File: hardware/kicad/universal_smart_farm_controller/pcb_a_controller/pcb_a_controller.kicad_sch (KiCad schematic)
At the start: 55 parts, among them J1 Conn_01x12, J19 Conn_01x03, J2 Conn_01x03, J3 Conn_01x04, J4 Conn_01x04, J5 Conn_01x03, J6 Conn_01x03, J7 Conn_01x03, J8 Conn_01x03, J9 Conn_01x04, SW1 RESET, SW2 BOOT, U1 ESP32-WROOM-32E, U2 ADS1115IDGS, U3 MAX3485ESA+, U4 TPS5430DDA, U5 AP2112K-3.3

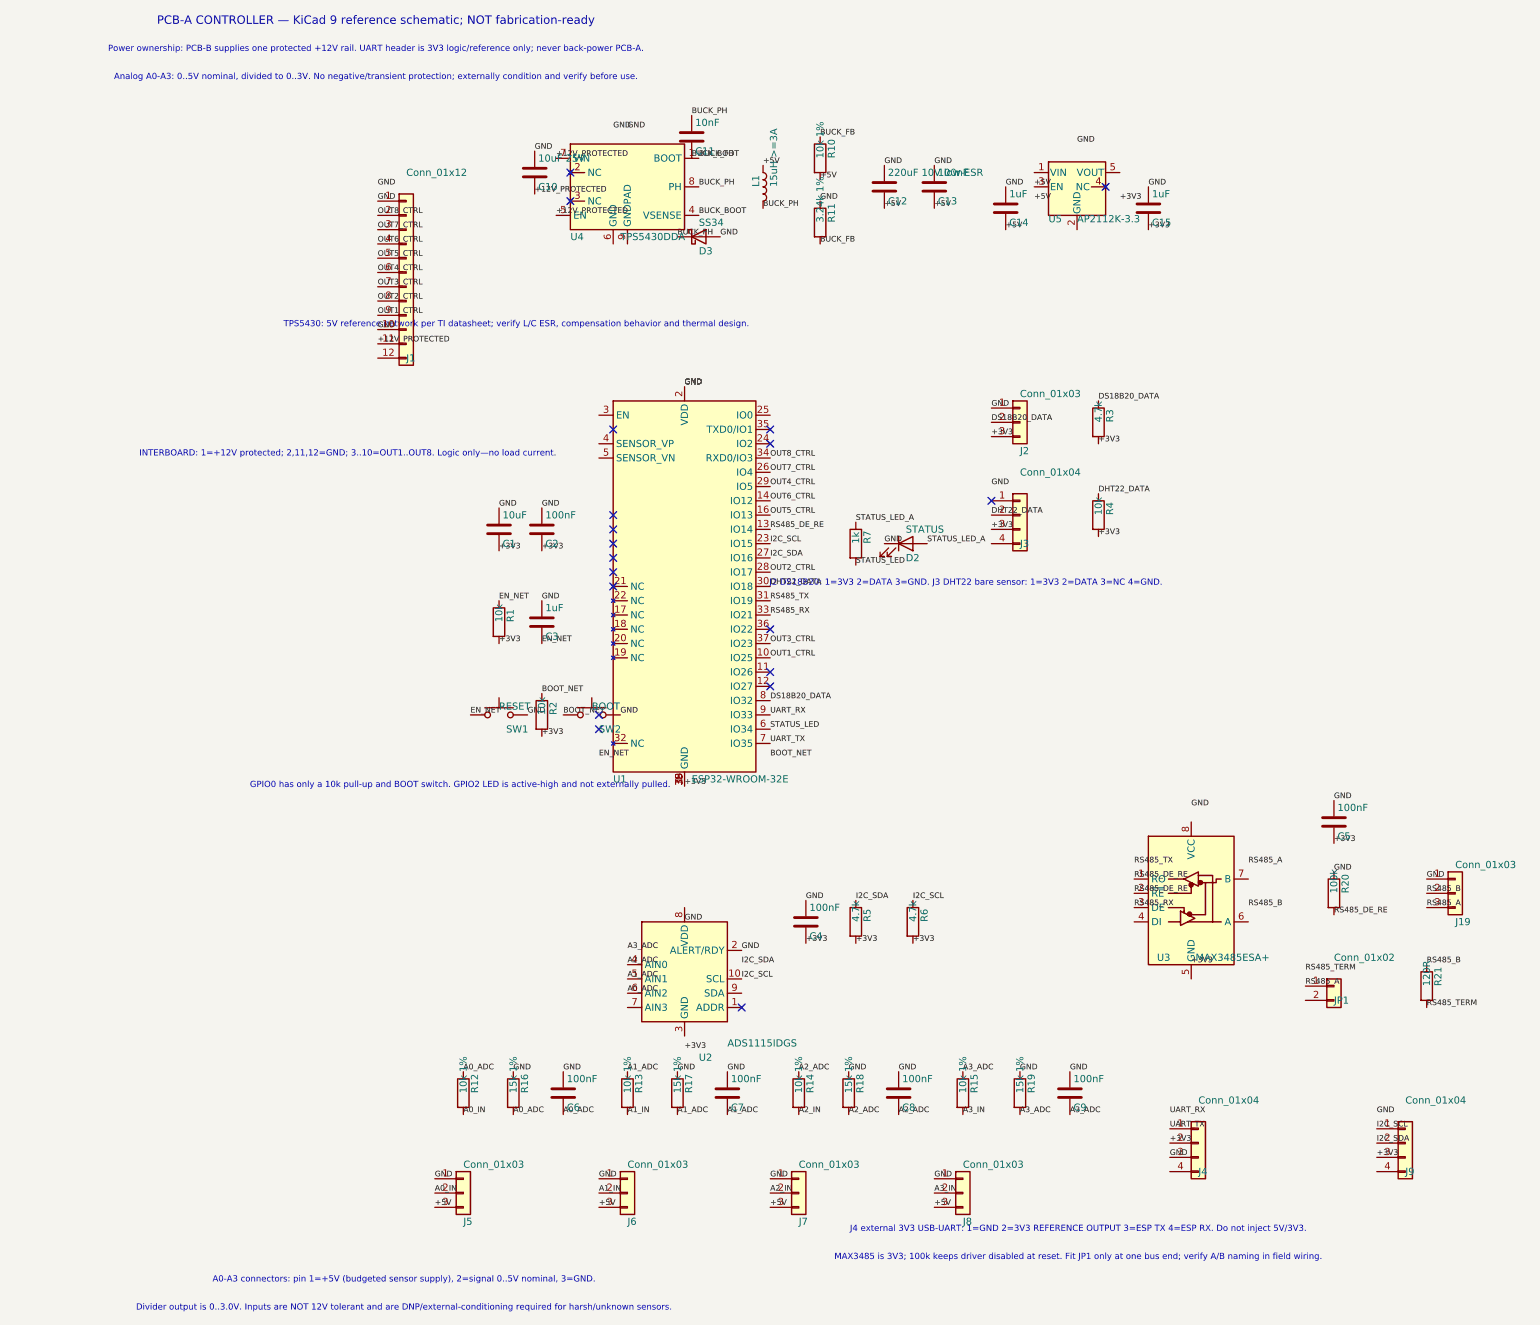
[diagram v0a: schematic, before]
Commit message: Place PCB-A footprints and antenna keepout with layout limits
Co-authored-by: tomnyle <175001228+tomnyle@users.noreply.github.com>
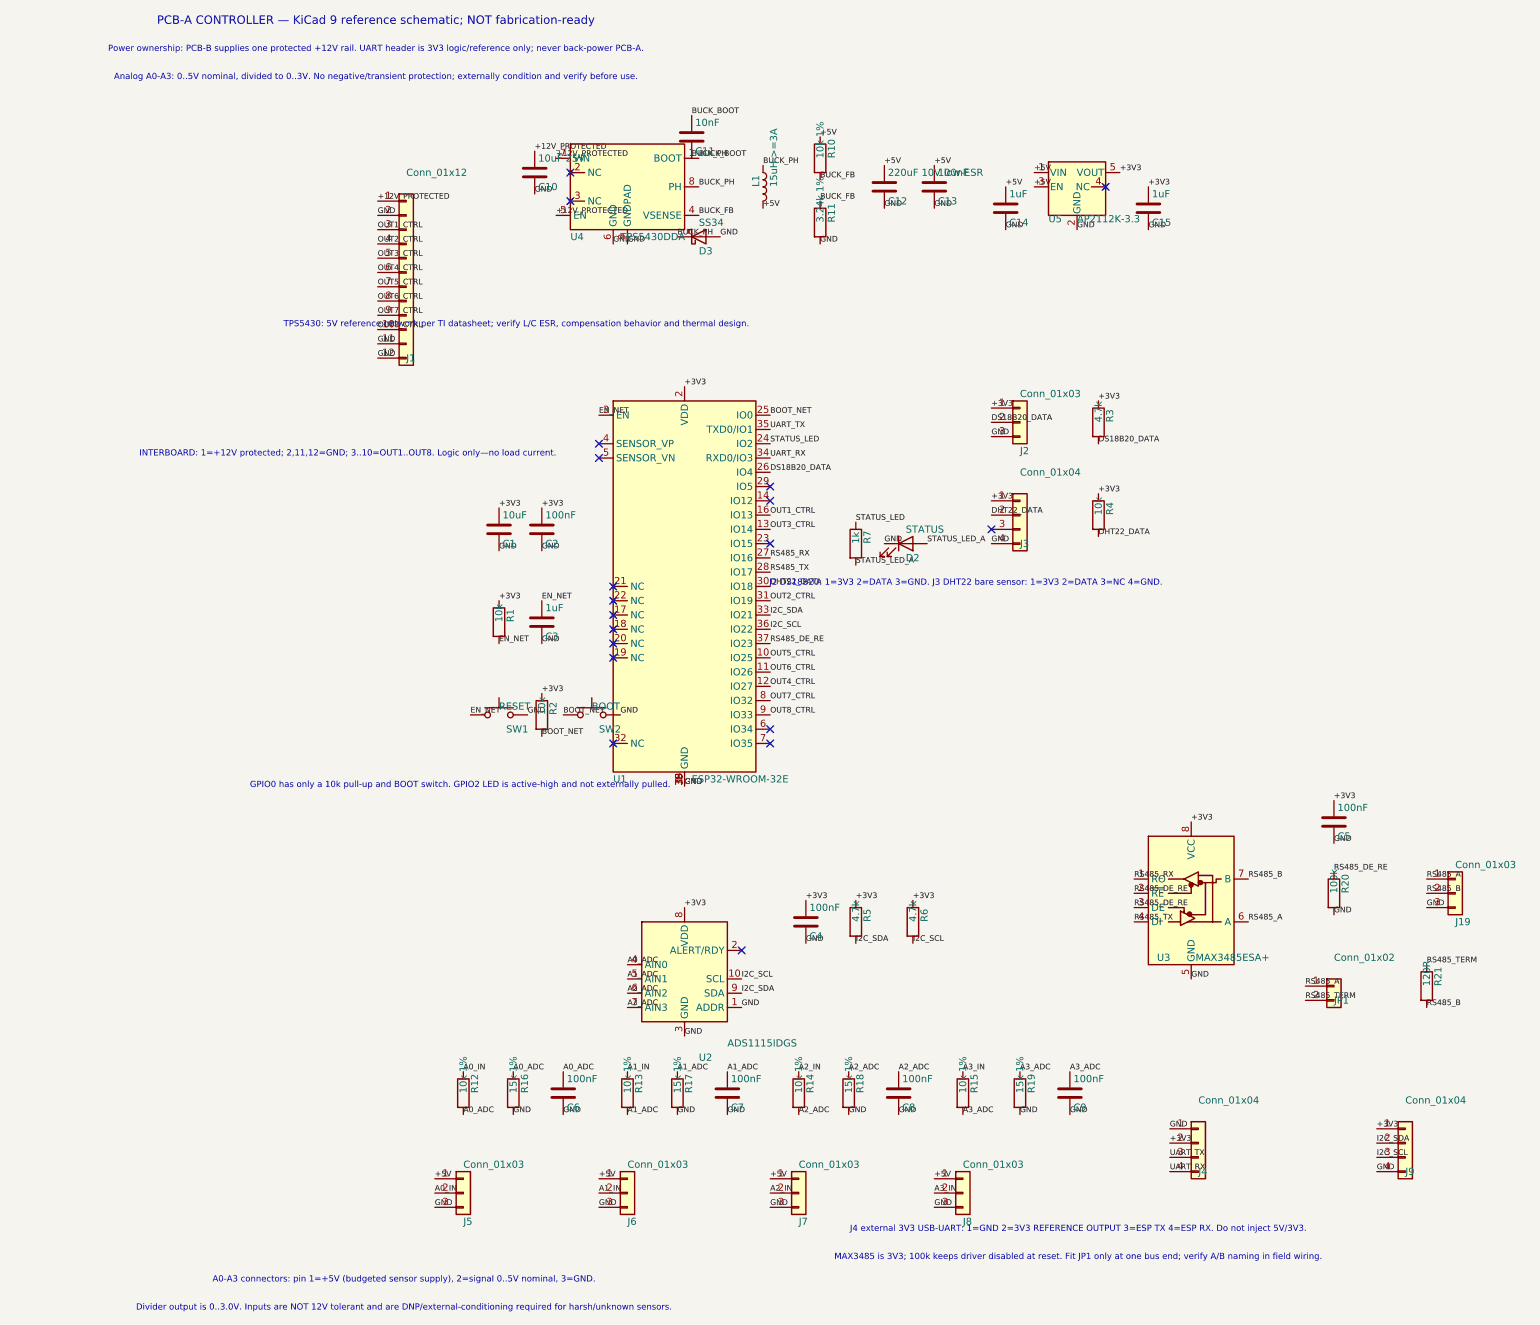
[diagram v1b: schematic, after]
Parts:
- J1: footprint Connector_PinHeader_2.54mm:PinHeader_2x06_P2.54mm_Vertical -> Connector_IDC:IDC-Header_2x06_P2.54mm_Vertical
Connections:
- net +12V_PROTECTED: now also C10.1, J1.1 (Pin_1); no longer C10.2, J1.11 (Pin_11)
- net +3V3: now also C1.1, C15.1, C2.1, C4.1, C5.1, J2.1 (Pin_1), J3.1 (Pin_1), J9.1 (Pin_1), R1.1, R2.1, R3.1, R4.1, R5.1, R6.1, U1.2 (VDD), U2.8 (VDD), U3.8 (VCC), U5.5 (VOUT); no longer C1.2, C15.2, C2.2, C4.2, C5.2, J2.3 (Pin_3), J3.3 (Pin_3), J9.3 (Pin_3), R1.2, R2.2, R3.2, R4.2, R5.2, R6.2, U1.1 (GND), U1.15 (GND), U1.38 (GND), U1.39 (GND)
- net +5V: now also C12.1, C13.1, C14.1, J5.1 (Pin_1), J6.1 (Pin_1), J7.1 (Pin_1), J8.1 (Pin_1), L1.2, R10.1, U5.1 (VIN); no longer C12.2, C13.2, C14.2, J5.3 (Pin_3), J6.3 (Pin_3), J7.3 (Pin_3), J8.3 (Pin_3), L1.1, R10.2
- net A0_ADC: now also C6.1, R12.2, R16.1, U2.4 (AIN0); no longer C6.2, R12.1, R16.2, U2.6 (AIN2)
- net A0_IN: now also R12.1; no longer R12.2
- net A1_ADC: now also C7.1, R13.2, R17.1; no longer C7.2, R13.1, R17.2
- net A1_IN: now also R13.1; no longer R13.2
- net A2_ADC: now also C8.1, R14.2, R18.1, U2.6 (AIN2); no longer C8.2, R14.1, R18.2, U2.4 (AIN0)
- net A2_IN: now also R14.1; no longer R14.2
- net A3_ADC: now also C9.1, R15.2, R19.1, U2.7 (AIN3); no longer C9.2, R15.1, R19.2
- net A3_IN: now also R15.1; no longer R15.2
- net BOOT_NET: now also R2.2, U1.25 (IO0); no longer R2.1
- net BUCK_BOOT: now also C11.1, U4.1 (BOOT); no longer C11.2, U4.4 (VSENSE)
- net BUCK_FB: now also R10.2, R11.1, U4.4 (VSENSE); no longer R10.1, R11.2, U4.1 (BOOT)
- net BUCK_PH: now also C11.2, L1.1; no longer C11.1, L1.2
- net DHT22_DATA: now also R4.2; no longer R4.1
- net DS18B20_DATA: now also R3.2, U1.26 (IO4); no longer R3.1, U1.8 (IO32)
- net EN_NET: now also C3.1, R1.2, U1.3 (EN); no longer C3.2, R1.1
- net GND: now also C1.2, C10.2, C12.2, C13.2, C14.2, C15.2, C2.2, C3.2, C4.2, C5.2, C6.2, C7.2, C8.2, C9.2, J1.11 (Pin_11), J1.12 (Pin_12), J1.2 (Pin_2), J19.3 (Pin_3), J2.3 (Pin_3), J3.4 (Pin_4), J4.1 (Pin_1), J5.3 (Pin_3), J6.3 (Pin_3), J7.3 (Pin_3), J8.3 (Pin_3), J9.4 (Pin_4), R11.2, R16.2, R17.2, R18.2, R19.2, R20.2, U1.1 (GND), U1.15 (GND), U1.38 (GND), U1.39 (GND), U2.1 (ADDR), U2.3 (GND), U3.5 (GND), U4.6 (GND), U4.9 (GNDPAD), U5.2 (GND); no longer C1.1, C10.1, C12.1, C13.1, C14.1, C15.1, C2.1, C3.1, C4.1, C5.1, C6.1, C7.1, C8.1, C9.1, J1.1 (Pin_1), J1.10 (Pin_10), J19.1 (Pin_1), J2.1 (Pin_1), J4.3 (Pin_3), J5.1 (Pin_1), J6.1 (Pin_1), J7.1 (Pin_1), J8.1 (Pin_1), R11.1, R16.1, R17.1, R18.1, R19.1, R20.1, U1.2 (VDD), U2.2 (ALERT/RDY)
- net I2C_SCL: now also J9.3 (Pin_3), R6.2, U1.36 (IO22); no longer J9.1 (Pin_1), R6.1, U1.23 (IO15)
- net I2C_SDA: now also R5.2, U1.33 (IO21), U2.9 (SDA); no longer R5.1, U1.27 (IO16)
- net OUT1_CTRL: now also J1.3 (Pin_3), U1.16 (IO13); no longer J1.9 (Pin_9), U1.10 (IO25)
- net OUT2_CTRL: now also J1.4 (Pin_4), U1.31 (IO19); no longer J1.8 (Pin_8), U1.28 (IO17)
- net OUT3_CTRL: now also J1.5 (Pin_5), U1.13 (IO14); no longer J1.7 (Pin_7), U1.37 (IO23)
- net OUT4_CTRL: now also U1.12 (IO27); no longer U1.29 (IO5)
- net OUT5_CTRL: now also J1.7 (Pin_7), U1.10 (IO25); no longer J1.5 (Pin_5), U1.16 (IO13)
- net OUT6_CTRL: now also J1.8 (Pin_8), U1.11 (IO26); no longer J1.4 (Pin_4), U1.14 (IO12)
- net OUT7_CTRL: now also J1.9 (Pin_9), U1.8 (IO32); no longer J1.3 (Pin_3), U1.26 (IO4)
- net OUT8_CTRL: now also J1.10 (Pin_10), U1.9 (IO33); no longer J1.2 (Pin_2), U1.34 (RXD0/IO3)
- net RS485_A: now also J19.1 (Pin_1), U3.6 (A); no longer J19.3 (Pin_3)
- net RS485_B: now also R21.2, U3.7 (B); no longer R21.1
- net RS485_DE_RE: now also R20.1, U1.37 (IO23), U3.3 (DE); no longer R20.2, U1.13 (IO14), U3.1 (RO)
- net RS485_RX: now also U1.27 (IO16), U3.1 (RO); no longer U1.33 (IO21), U3.3 (DE)
- net RS485_TERM: now also JP1.2 (Pin_2), R21.1; no longer R21.2
- net RS485_TX: now also U1.28 (IO17), U3.4 (DI); no longer U1.31 (IO19)
- net STATUS_LED: now also R7.1, U1.24 (IO2); no longer R7.2, U1.6 (IO34)
- net STATUS_LED_A: now also R7.2; no longer R7.1
- net UART_RX: now also J4.4 (Pin_4), U1.34 (RXD0/IO3); no longer U1.9 (IO33)
- net UART_TX: now also J4.3 (Pin_3), U1.35 (TXD0/IO1); no longer J4.1 (Pin_1), U1.7 (IO35)
